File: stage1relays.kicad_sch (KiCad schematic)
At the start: 17 parts, among them T3 AO3400A, T4 AO3400A, T7 AO3400A

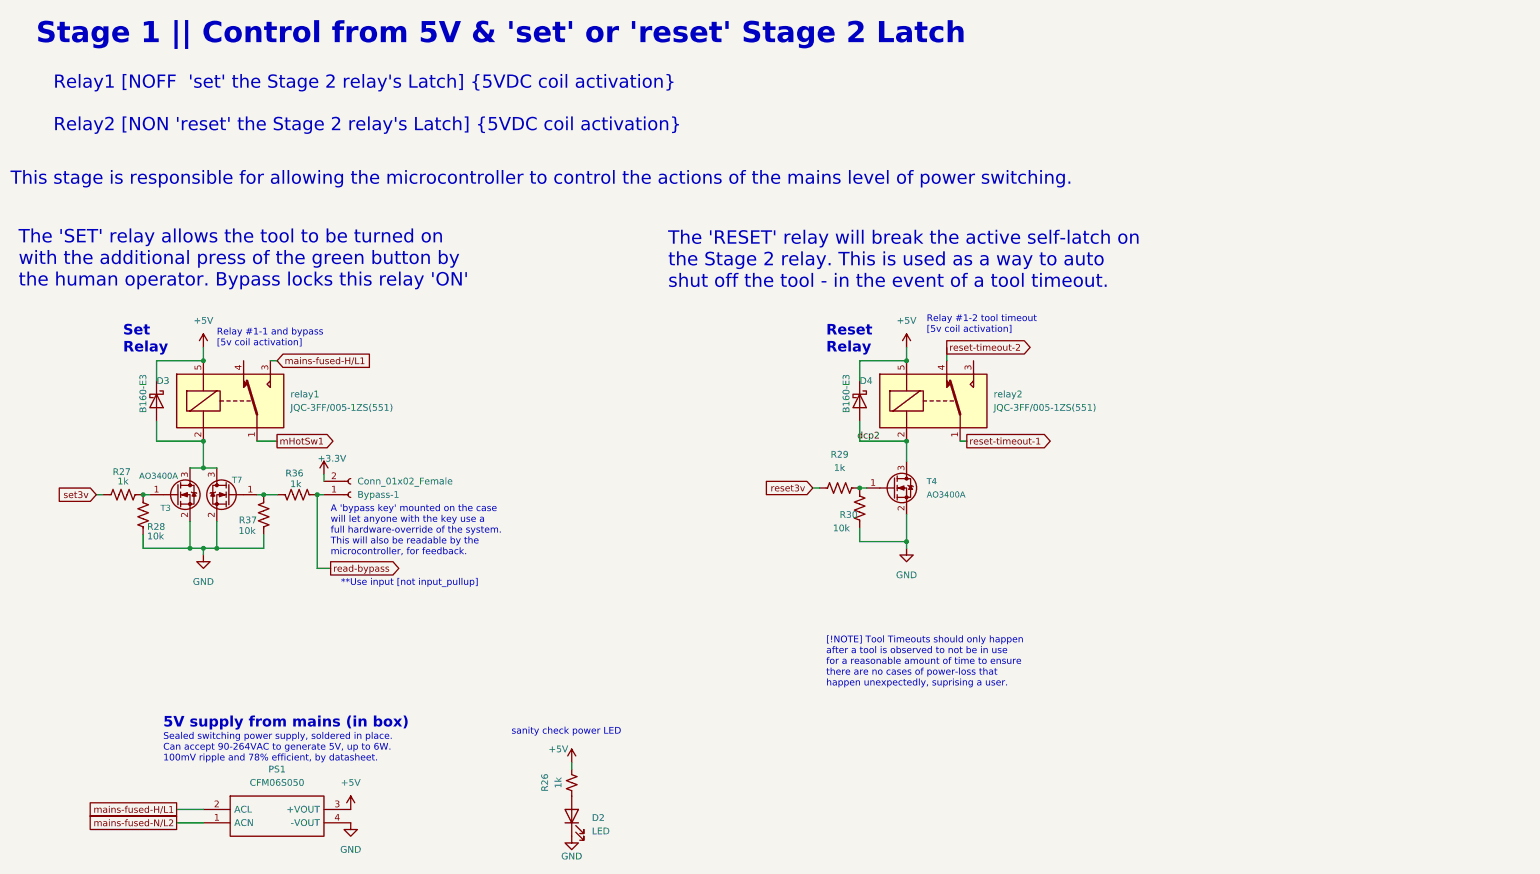
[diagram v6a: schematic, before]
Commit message: moved LED GPIO to fit free pins for ethernet wing
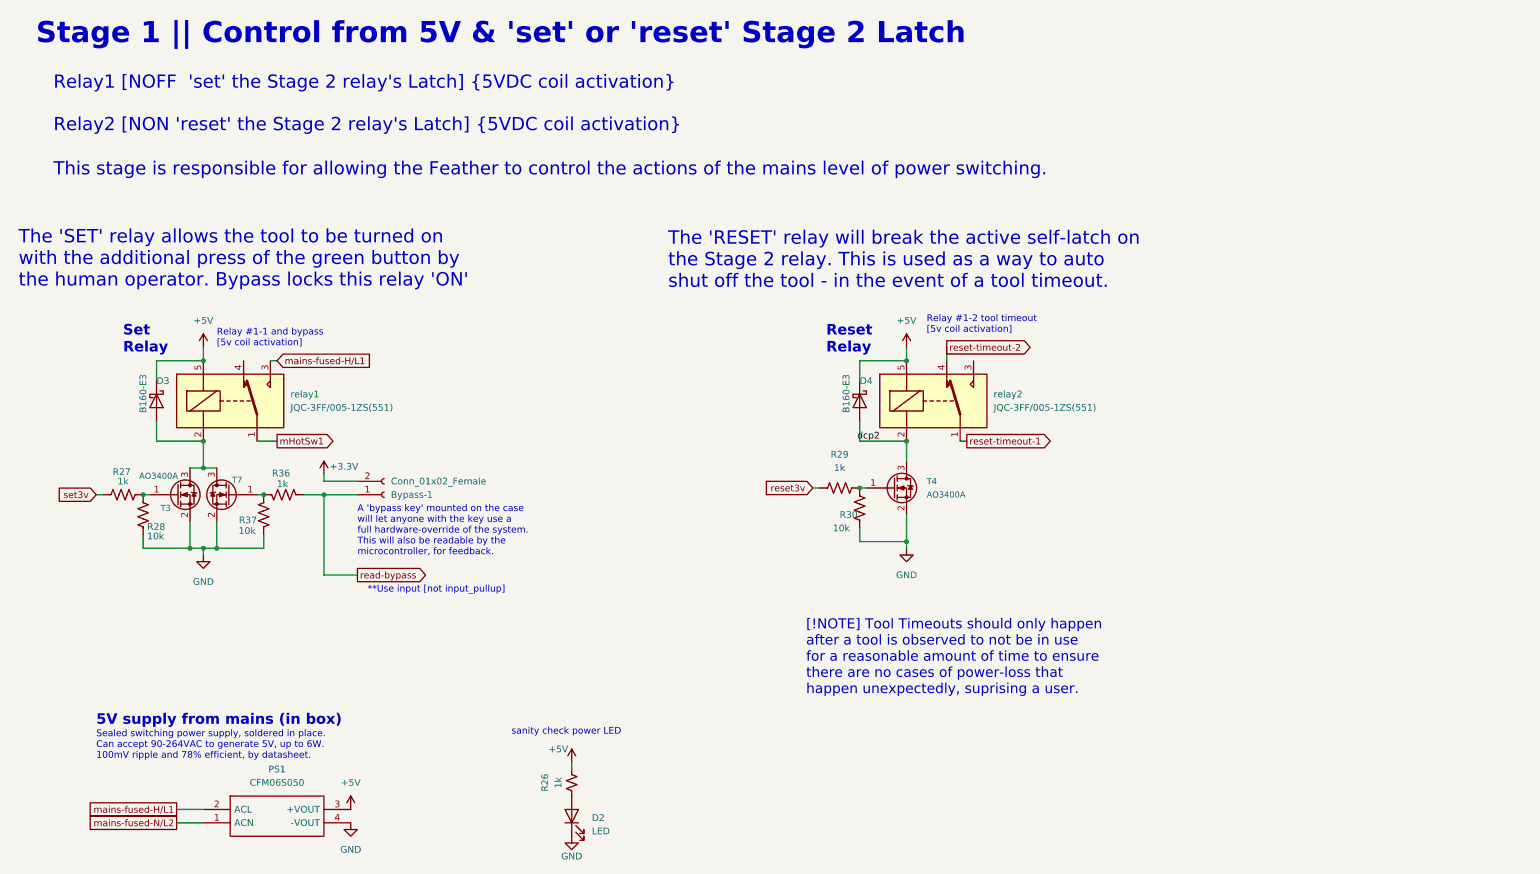
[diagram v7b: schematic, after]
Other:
- note added: "This stage is responsible for allowing the Feather to control the actions of the mains level of power switching."
- note removed: "This stage is responsible for allowing the microcontroller to control the actions of the mains level of power switching."
- moved on the sheet: Bypass-1, R36
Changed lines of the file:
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@@
 	)
 	(junction
-		(at 81.28 114.3)
+		(at 82.55 114.3)
 		(diameter 0)
 		(color 0 0 0 0)
@@
 	(wire
 		(pts
-			(xy 81.28 114.3) (xy 82.55 114.3)
+			(xy 82.55 114.3) (xy 88.9 114.3)
+		)
+		(stroke
+			(width 0)
+			(type default)
+		)
+	)
+	(wire
+		(pts
+			(xy 78.74 114.3) (xy 82.55 114.3)
 		)
 		(stroke
@@
 	(wire
 		(pts
+			(xy 82.55 111.76) (xy 88.9 111.76)
+		)
+		(stroke
+			(width 0)
+			(type default)
+		)
+	)
+	(wire
+		(pts
 			(xy 184.15 104.14) (xy 184.15 100.33)
 		)
@@
 	(wire
 		(pts
-			(xy 73.66 114.3) (xy 71.12 114.3)
-		)
-		(stroke
-			(width 0)
-			(type default)
-		)
-	)
-	(wire
-		(pts
-			(xy 81.28 114.3) (xy 81.28 128.27)
-		)
-		(stroke
-			(width 0)
-			(type default)
-		)
-	)
-	(wire
-		(pts
-			(xy 81.28 128.27) (xy 83.82 128.27)
+			(xy 82.55 114.3) (xy 82.55 129.54)
+		)
+		(stroke
+			(width 0)
+			(type default)
+		)
+	)
+	(wire
+		(pts
+			(xy 82.55 129.54) (xy 88.9 129.54)
 		)
 		(stroke
@@
 	(text "**Use input [not input_pullup]"
 		(exclude_from_sim no)
-		(at 98.806 131.064 0)
+		(at 103.886 132.334 0)
 		(effects
 			(font
@@
 	(text "Sealed switching power supply, soldered in place.\nCan accept 90-264VAC to generate 5V, up to 6W.\n100mV ripple and 78% efficient, by datasheet."
 		(exclude_from_sim no)
-		(at 52.07 165.1 0)
+		(at 39.37 164.592 0)
 		(effects
 			(font
@@
 	(text "[!NOTE] Tool Timeouts should only happen\nafter a tool is observed to not be in use \nfor a reasonable amount of time to ensure \nthere are no cases of power-loss that \nhappen unexpectedly, suprising a user.\n"
 		(exclude_from_sim no)
-		(at 177.8 150.876 0)
+		(at 173.99 152.4 0)
+		(effects
+			(font
+				(size 1.905 1.905)
+			)
+			(justify left bottom)
+		)
+	)
+	(text "A 'bypass key' mounted on the case \nwill let anyone with the key use a \nfull hardware-override of the system. \nThis will also be readable by the \nmicrocontroller, for feedback."
+		(exclude_from_sim no)
+		(at 88.9 125.984 0)
 		(effects
 			(font
@@
 		)
 	)
-	(text "A 'bypass key' mounted on the case \nwill let anyone with the key use a \nfull hardware-override of the system. \nThis will also be readable by the \nmicrocontroller, for feedback."
-		(exclude_from_sim no)
-		(at 83.82 125.984 0)
-		(effects
-			(font
-				(size 1.27 1.27)
+	(text "This stage is responsible for allowing the Feather to control the actions of the mains level of power switching."
+		(exclude_from_sim no)
+		(at 31.242 54.102 0)
+		(effects
+			(font
+				(size 2.5 2.5)
 			)
 			(justify left bottom)
 		)
 	)
-	(text "This stage is responsible for allowing the microcontroller to control the actions of the mains level of power switching."
-		(exclude_from_sim no)
-		(at 23.114 55.88 0)
-		(effects
-			(font
-				(size 2.5 2.5)
-			)
-			(justify left bottom)
-		)
-	)
 	(text "5V supply from mains (in box)"
 		(exclude_from_sim no)
-		(at 52.07 158.75 0)
+		(at 39.37 158.242 0)
 		(effects
 			(font
@@
 	(global_label "read-bypass"
 		(shape output)
-		(at 83.82 128.27 0)
+		(at 88.9 129.54 0)
 		(fields_autoplaced yes)
 		(effects
@@
 		)
 		(property "Intersheetrefs" "${INTERSHEET_REFS}"
-			(at 98.4493 128.1906 0)
+			(at 103.5293 129.4606 0)
 			(effects
 				(font
@@
 		(length 2.54)
 		(shape round)
-		(at 81.28 128.27 180)
+		(at 82.55 129.54 90)
 		(fields_autoplaced yes)
 		(effects
@@
 				(size 1.27 1.27)
 			)
-			(justify right bottom)
+			(justify left bottom)
 		)
 		(property "Netclass" "Default"
-			(at 80.5815 130.81 0)
+			(at 80.01 128.8415 90)
 			(effects
 				(font
@@
 					(italic yes)
 				)
-				(justify right)
+				(justify left)
 			)
 		)
@@
 		)
 		(property "Value" "+3.3V"
-			(at 84.074 107.442 0)
+			(at 86.36 108.966 0)
 			(effects
 				(font
@@
 	(symbol
 		(lib_id "Device:R_US")
-		(at 77.47 114.3 270)
+		(at 74.93 114.3 270)
 		(mirror x)
 		(unit 1)
@@
 		(dnp no)
 		(property "Reference" "R36"
-			(at 76.962 110.236 90)
+			(at 74.422 110.236 90)
 			(effects
 				(font
@@
 		)
 		(property "Value" "1k"
-			(at 77.216 112.268 90)
+			(at 74.676 112.268 90)
 			(effects
 				(font
@@
 		)
 		(property "Footprint" "Resistor_SMD:R_0603_1608Metric"
-			(at 77.216 113.284 90)
+			(at 74.676 113.284 90)
 			(effects
 				(font
@@
 		)
 		(property "Datasheet" "~"
-			(at 77.47 114.3 0)
+			(at 74.93 114.3 0)
 			(effects
 				(font
@@
 		)
 		(property "Description" ""
-			(at 77.47 114.3 0)
+			(at 74.93 114.3 0)
 			(effects
 				(font
@@
 		)
 		(property "JLCPCB Part #" "C21190"
-			(at 77.47 114.3 90)
+			(at 74.93 114.3 90)
 			(effects
 				(font
@@
 	(symbol
 		(lib_id "Connector:Conn_01x02_Female")
-		(at 87.63 114.3 0)
+		(at 93.98 114.3 0)
 		(mirror x)
 		(unit 1)
@@
 		(dnp no)
 		(property "Reference" "Bypass-1"
-			(at 88.9 114.3001 0)
+			(at 95.25 114.3001 0)
 			(effects
 				(font
@@
 		)
 		(property "Value" "Conn_01x02_Female"
-			(at 88.9 111.7601 0)
+			(at 95.25 111.7601 0)
 			(effects
 				(font
@@
 		)
 		(property "Footprint" "Connector_JST:JST_PH_B2B-PH-K_1x02_P2.00mm_Vertical"
-			(at 87.63 114.3 0)
+			(at 93.98 114.3 0)
 			(effects
 				(font
@@
 		)
 		(property "Datasheet" "~"
-			(at 87.63 114.3 0)
+			(at 93.98 114.3 0)
 			(effects
 				(font
@@
 		)
 		(property "Description" ""
-			(at 87.63 114.3 0)
+			(at 93.98 114.3 0)
 			(effects
 				(font
@@
 		)
 		(property "JLCPCB Part #" "C131337"
-			(at 87.63 114.3 0)
-			(effects
-				(font
+			(at 93.98 114.3 0)
+			(effects
+				(font

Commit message: ordered B1P3 test run from JLCPCB
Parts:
- D3, D4: value B160-E3 -> SS14; symbol Diode:B160-E3 -> Diode:SS14; JLCPCB Part # C24784 -> C2480
- PS1: now left out of the parts list
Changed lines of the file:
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@@
 		(unit 1)
 		(exclude_from_sim no)
-		(in_bom yes)
+		(in_bom no)
 		(on_board yes)
 		(dnp no)
@@
 	)
 	(symbol
-		(lib_id "Diode:B160-E3")
+		(lib_id "Diode:SS14")
 		(at 50.8 96.52 270)
 		(unit 1)
@@
 			)
 		)
-		(property "Value" "B160-E3"
-			(at 48.26 91.44 0)
-			(effects
-				(font
-					(size 1.27 1.27)
-				)
-				(justify left)
+		(property "Value" "SS14"
+			(at 48.26 96.52 0)
+			(effects
+				(font
+					(size 1.27 1.27)
+				)
 			)
 		)
@@
 			)
 		)
-		(property "Datasheet" "http://www.vishay.com/docs/88946/b120.pdf"
+		(property "Datasheet" "https://www.vishay.com/docs/88746/ss12.pdf"
 			(at 50.8 96.52 0)
 			(effects
@@
 			)
 		)
-		(property "Description" ""
+		(property "Description" "40V 1A Schottky Diode, SMA"
 			(at 50.8 96.52 0)
 			(effects
@@
 			)
 		)
-		(property "JLCPCB Part #" "C24784"
+		(property "JLCPCB Part #" "C2480"
 			(at 50.8 96.52 90)
 			(effects
@@
 	)
 	(symbol
-		(lib_id "Diode:B160-E3")
+		(lib_id "Diode:SS14")
 		(at 184.15 96.52 270)
 		(unit 1)
@@
 			)
 		)
-		(property "Value" "B160-E3"
-			(at 181.61 91.44 0)
-			(effects
-				(font
-					(size 1.27 1.27)
-				)
-				(justify left)
+		(property "Value" "SS14"
+			(at 181.61 96.52 0)
+			(effects
+				(font
+					(size 1.27 1.27)
+				)
 			)
 		)
@@
 			)
 		)
-		(property "Datasheet" "http://www.vishay.com/docs/88946/b120.pdf"
+		(property "Datasheet" "https://www.vishay.com/docs/88746/ss12.pdf"
 			(at 184.15 96.52 0)
 			(effects
@@
 			)
 		)
-		(property "Description" ""
+		(property "Description" "40V 1A Schottky Diode, SMA"
 			(at 184.15 96.52 0)
 			(effects
@@
 			)
 		)
-		(property "JLCPCB Part #" "C24784"
+		(property "JLCPCB Part #" "C2480"
 			(at 184.15 96.52 90)
 			(effects
